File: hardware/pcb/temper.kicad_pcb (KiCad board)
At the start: 2 copper layers, 111.3 x 90 mm, 48 parts, among them J2 nice_view, SW1 SW_PUSH, SW10 SW_PUSH, SW11 SW_PUSH, SW12 SW_PUSH, SW13 SW_PUSH, SW14 SW_PUSH, SW15 SW_PUSH, SW16 SW_PUSH, SW17 SW_PUSH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

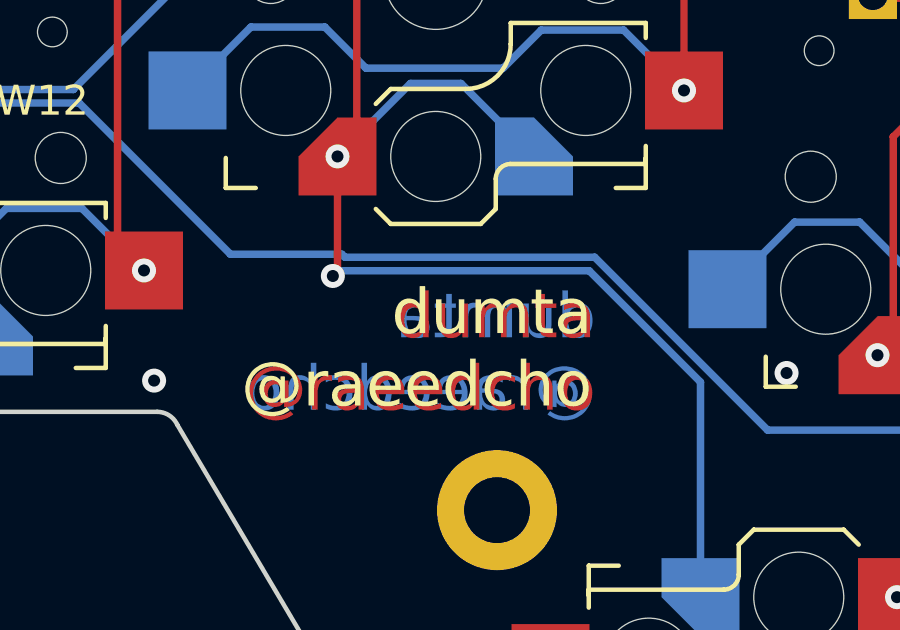
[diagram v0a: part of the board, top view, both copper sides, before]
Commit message: refactor: rename kicad project to temper, keeping the library name the same
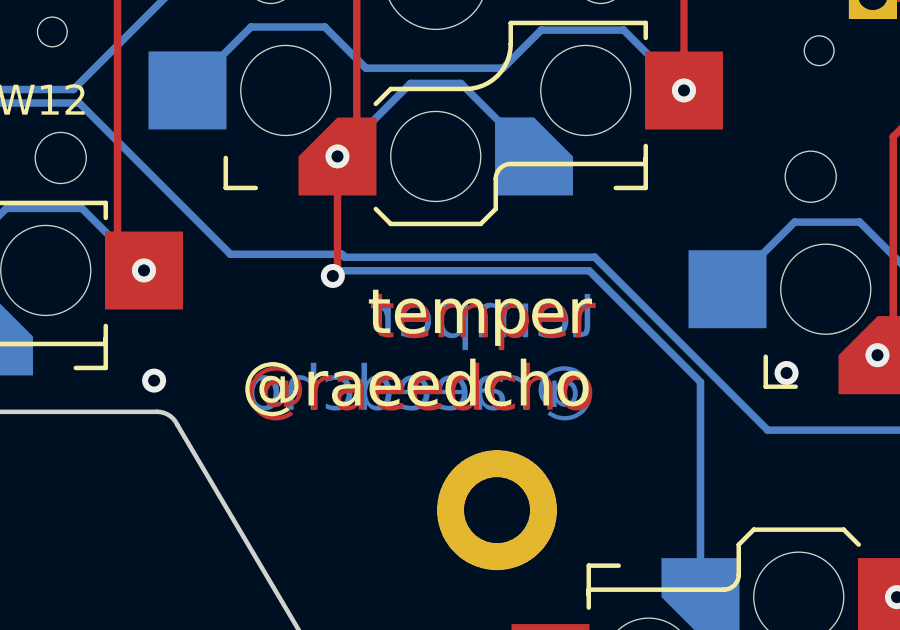
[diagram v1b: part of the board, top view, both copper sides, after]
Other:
- board text added: "temper @raeedcho"
- board text removed: "dumta @raeedcho"
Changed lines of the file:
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@@
   (paper "A4")
   (title_block
-    (title "dumta")
-    (date "2023-07-10")
+    (title "temper")
+    (date "2023-07-14")
     (rev "1.0")
     (company "raeedcho")
@@
       (psa4output false)
       (plotreference true)
-      (plotvalue true)
+      (plotvalue false)
       (plotinvisibletext false)
       (sketchpadsonfab false)
@@
     (fp_arc (start -2.5 6.2) (mid -2.146447 6.346447) (end -2 6.7)
       (stroke (width 0.15) (type solid)) (layer "B.SilkS"))
-    (fp_arc (start -1 3.7) (mid -2.06066 3.26066) (end -2.5 2.2)
+    (fp_arc (start -1 3.7) (mid -2.06066 3.260659) (end -2.5 2.2)
       (stroke (width 0.15) (type solid)) (layer "B.SilkS"))
     (fp_line (start -7 -7) (end -6 -7)
@@
     (fp_arc (start -2.5 6.2) (mid -2.146447 6.346447) (end -2 6.7)
       (stroke (width 0.15) (type solid)) (layer "B.Fab"))
-    (fp_arc (start -1 3.7) (mid -2.06066 3.26066) (end -2.5 2.2)
+    (fp_arc (start -1 3.7) (mid -2.06066 3.260659) (end -2.5 2.2)
       (stroke (width 0.15) (type solid)) (layer "B.Fab"))
     (fp_line (start -7.5 -7.5) (end 7.5 -7.5)
@@
   (gr_arc (start 77.6732 112.776) (mid 77.206227 112.582573) (end 77.0128 112.1156)
     (stroke (width 0.15) (type solid)) (layer "Edge.Cuts"))
-  (gr_text "dumta\n@raeedcho" (at 127.24 98.89) (layer "F.Cu")
+  (gr_text "temper\n@raeedcho" (at 127.24 98.89) (layer "F.Cu")
     (effects (font (size 1.5 1.5) (thickness 0.3)) (justify right))
   )
-  (gr_text "dumta\n@raeedcho" (at 127.25 98.89) (layer "B.Cu")
+  (gr_text "temper\n@raeedcho" (at 127.25 98.89) (layer "B.Cu")
     (effects (font (size 1.5 1.5) (thickness 0.3)) (justify left mirror))
   )
-  (gr_text "dumta\n@raeedcho" (at 127.13 98.75) (layer "B.SilkS")
+  (gr_text "temper\n@raeedcho" (at 127.13 98.75) (layer "B.SilkS")
     (effects (font (size 1.5 1.5) (thickness 0.3)) (justify left mirror))
   )
-  (gr_text "dumta\n@raeedcho" (at 127.12 98.75) (layer "F.SilkS")
+  (gr_text "temper\n@raeedcho" (at 127.12 98.75) (layer "F.SilkS")
     (effects (font (size 1.5 1.5) (thickness 0.3)) (justify right))
   )
